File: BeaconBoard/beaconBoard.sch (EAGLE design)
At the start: 32 parts, among them IC1 7805TV, Q1 2N3904

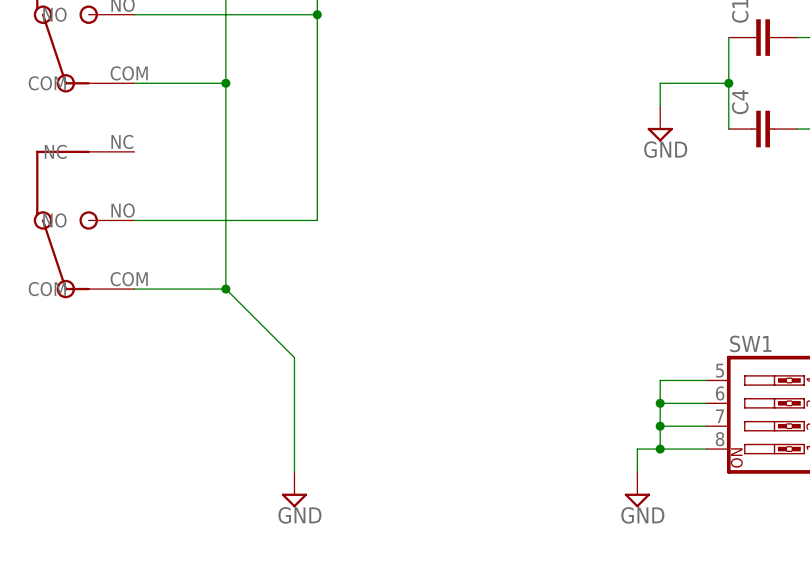
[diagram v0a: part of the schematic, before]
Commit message: Add pull up resistor to bumpers
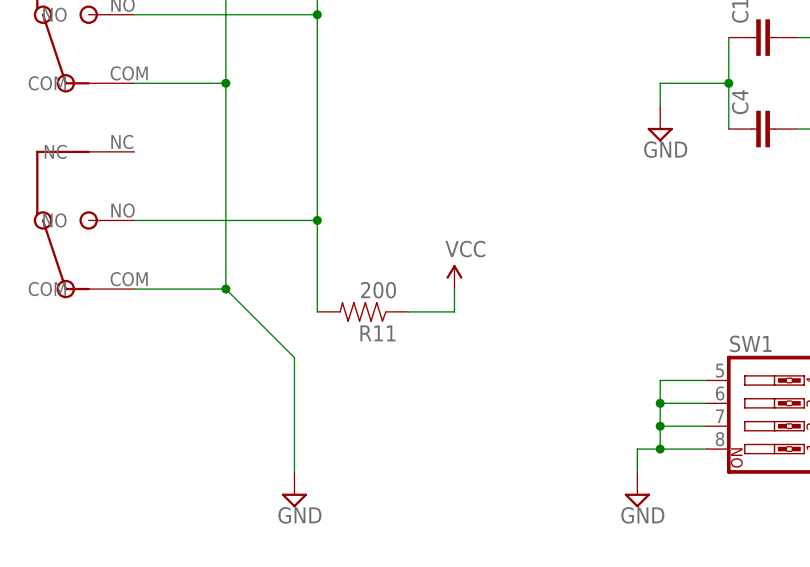
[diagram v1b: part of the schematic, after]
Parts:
- added R11: 200, SparkFun-Resistors:RESISTORPTH-1/4W
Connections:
- net BUMPER: now also R11.2
- net VCC: now also R11.1
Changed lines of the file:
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@@
 <part name="SUPPLY10" library="supply2" deviceset="GND" device=""/>
 <part name="SUPPLY11" library="supply2" deviceset="GND" device=""/>
+<part name="V_OUT6" library="SparkFun-Aesthetics" deviceset="VCC" device=""/>
+<part name="R11" library="SparkFun-Resistors" deviceset="RESISTOR" device="PTH-1/4W" value="200"/>
 </parts>
 <sheets>
@@
 <instance part="SUPPLY10" gate="GND" x="264.16" y="7.62"/>
 <instance part="SUPPLY11" gate="GND" x="17.78" y="-22.86"/>
+<instance part="V_OUT6" gate="1" x="35.56" y="0"/>
+<instance part="R11" gate="G$1" x="25.4" y="-2.54" rot="R180"/>
 </instances>
 <busses>
@@
 <wire x1="198.12" y1="116.84" x2="198.12" y2="114.3" width="0.1524" layer="91"/>
 <junction x="198.12" y="114.3"/>
+</segment>
+<segment>
+<pinref part="R11" gate="G$1" pin="1"/>
+<pinref part="V_OUT6" gate="1" pin="VCC"/>
+<wire x1="30.48" y1="-2.54" x2="35.56" y2="-2.54" width="0.1524" layer="91"/>
+<wire x1="35.56" y1="-2.54" x2="35.56" y2="0" width="0.1524" layer="91"/>
 </segment>
 </net>
@@
 <wire x1="20.32" y1="58.42" x2="38.1" y2="58.42" width="0.1524" layer="91"/>
 <label x="38.1" y="58.42" size="1.778" layer="95"/>
-</segment>
-<segment>
+<pinref part="R11" gate="G$1" pin="2"/>
+<wire x1="20.32" y1="-2.54" x2="20.32" y2="7.62" width="0.1524" layer="91"/>
+<junction x="20.32" y="7.62"/>
+</segment>
+<segment>

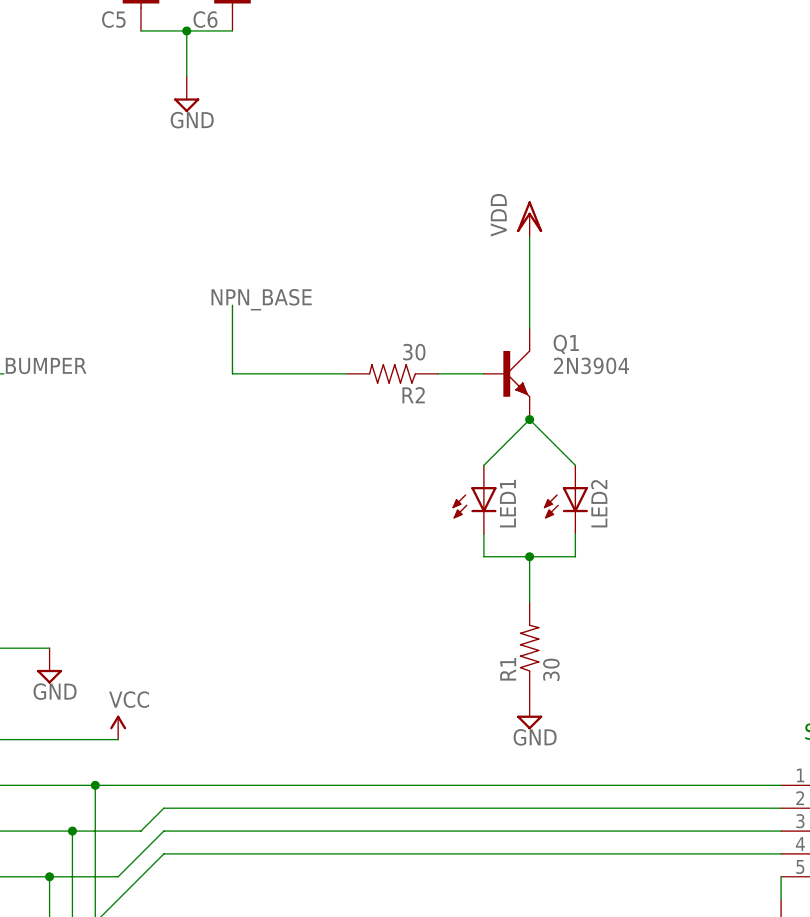
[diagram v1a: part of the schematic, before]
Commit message: Move leds above npn transistor
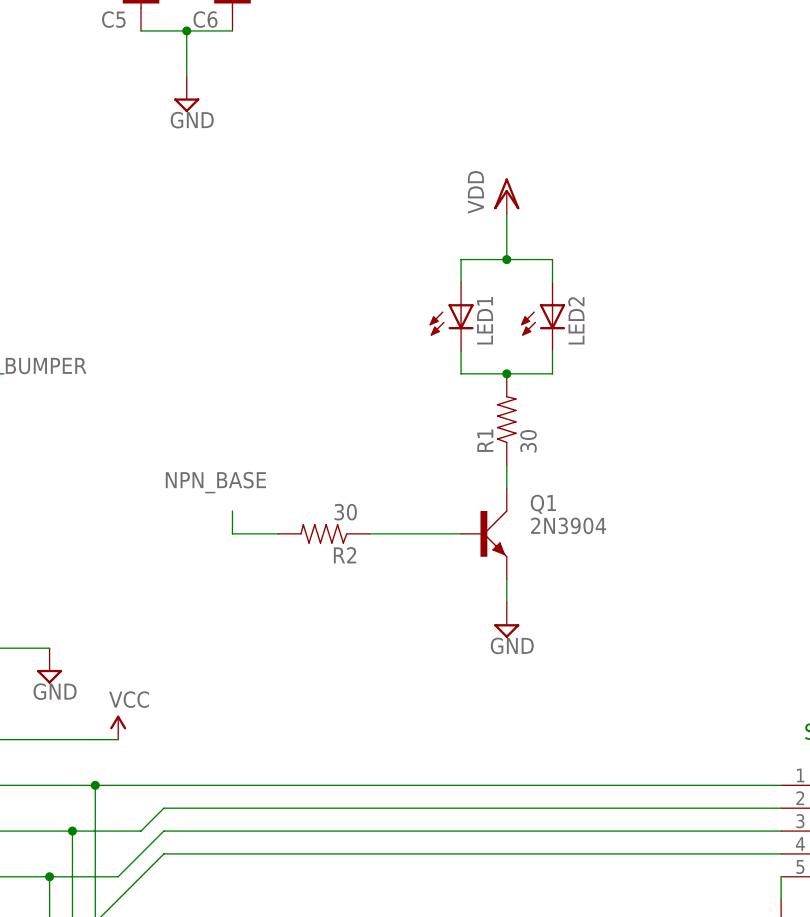
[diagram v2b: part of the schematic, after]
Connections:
- net GND: now also Q1.E; no longer R1.1
- net N$1: now also Q1.C, R1.1; no longer LED1.A, LED2.A, Q1.E
- net VDD: now also LED1.A, LED2.A; no longer Q1.C
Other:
- moved on the sheet: LED1, LED2, Q1, R1, R2
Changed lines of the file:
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@@
 <instance part="U$3" gate="G$1" x="0" y="45.72" rot="R90"/>
 <instance part="U$4" gate="G$1" x="124.46" y="-2.54"/>
-<instance part="Q1" gate="1" x="233.68" y="68.58"/>
+<instance part="Q1" gate="1" x="231.14" y="50.8"/>
 <instance part="J1" gate="G$1" x="-33.02" y="111.76"/>
 <instance part="IC1" gate="A1" x="30.48" y="93.98"/>
@@
 <instance part="V_OUT2" gate="1" x="190.5" y="27.94"/>
 <instance part="SUPPLY3" gate="GND" x="182.88" y="35.56"/>
-<instance part="LED1" gate="G$1" x="231.14" y="55.88"/>
-<instance part="LED2" gate="G$1" x="241.3" y="55.88"/>
-<instance part="SUPPLY4" gate="GND" x="236.22" y="30.48"/>
-<instance part="R1" gate="G$1" x="236.22" y="38.1" rot="R90"/>
-<instance part="R2" gate="G$1" x="220.98" y="68.58" rot="R180"/>
-<instance part="VDD2" gate="G$1" x="236.22" y="86.36"/>
+<instance part="LED1" gate="G$1" x="228.6" y="76.2"/>
+<instance part="LED2" gate="G$1" x="238.76" y="76.2"/>
+<instance part="SUPPLY4" gate="GND" x="233.68" y="40.64"/>
+<instance part="R1" gate="G$1" x="233.68" y="63.5" rot="R90"/>
+<instance part="R2" gate="G$1" x="213.36" y="50.8" rot="R180"/>
+<instance part="VDD2" gate="G$1" x="233.68" y="88.9"/>
 <instance part="R3" gate="G$1" x="193.04" y="-7.62" rot="R180"/>
 <instance part="R4" gate="G$1" x="193.04" y="-15.24" rot="R180"/>
@@
 </segment>
 <segment>
-<pinref part="Q1" gate="1" pin="C"/>
 <pinref part="VDD2" gate="G$1" pin="VDD"/>
-<wire x1="236.22" y1="83.82" x2="236.22" y2="73.66" width="0.1524" layer="91"/>
+<wire x1="233.68" y1="86.36" x2="233.68" y2="81.28" width="0.1524" layer="91"/>
+<wire x1="233.68" y1="81.28" x2="228.6" y2="81.28" width="0.1524" layer="91"/>
+<pinref part="LED1" gate="G$1" pin="A"/>
+<wire x1="228.6" y1="81.28" x2="228.6" y2="78.74" width="0.1524" layer="91"/>
+<pinref part="LED2" gate="G$1" pin="A"/>
+<wire x1="233.68" y1="81.28" x2="238.76" y2="81.28" width="0.1524" layer="91"/>
+<wire x1="238.76" y1="81.28" x2="238.76" y2="78.74" width="0.1524" layer="91"/>
+<junction x="233.68" y="81.28"/>
 </segment>
 </net>
@@
 <pinref part="U$4" gate="G$1" pin="GND@22"/>
 <wire x1="182.88" y1="38.1" x2="172.72" y2="38.1" width="0.1524" layer="91"/>
-</segment>
-<segment>
-<pinref part="SUPPLY4" gate="GND" pin="GND"/>
-<pinref part="R1" gate="G$1" pin="1"/>
 </segment>
 <segment>
@@
 <junction x="10.16" y="22.86"/>
 </segment>
-</net>
-<net name="N$1" class="0">
 <segment>
 <pinref part="Q1" gate="1" pin="E"/>
-<pinref part="LED1" gate="G$1" pin="A"/>
-<wire x1="236.22" y1="63.5" x2="231.14" y2="58.42" width="0.1524" layer="91"/>
-<pinref part="LED2" gate="G$1" pin="A"/>
-<wire x1="236.22" y1="63.5" x2="241.3" y2="58.42" width="0.1524" layer="91"/>
-<junction x="236.22" y="63.5"/>
+<pinref part="SUPPLY4" gate="GND" pin="GND"/>
+<wire x1="233.68" y1="43.18" x2="233.68" y2="45.72" width="0.1524" layer="91"/>
 </segment>
 </net>
@@
 <segment>
 <pinref part="LED1" gate="G$1" pin="C"/>
-<wire x1="231.14" y1="50.8" x2="231.14" y2="48.26" width="0.1524" layer="91"/>
+<wire x1="228.6" y1="71.12" x2="228.6" y2="68.58" width="0.1524" layer="91"/>
 <pinref part="LED2" gate="G$1" pin="C"/>
-<wire x1="241.3" y1="48.26" x2="241.3" y2="50.8" width="0.1524" layer="91"/>
-<wire x1="241.3" y1="48.26" x2="236.22" y2="48.26" width="0.1524" layer="91"/>
+<wire x1="238.76" y1="68.58" x2="238.76" y2="71.12" width="0.1524" layer="91"/>
+<wire x1="238.76" y1="68.58" x2="233.68" y2="68.58" width="0.1524" layer="91"/>
 <pinref part="R1" gate="G$1" pin="2"/>
-<wire x1="236.22" y1="48.26" x2="231.14" y2="48.26" width="0.1524" layer="91"/>
-<wire x1="236.22" y1="43.18" x2="236.22" y2="48.26" width="0.1524" layer="91"/>
-<junction x="236.22" y="48.26"/>
+<wire x1="233.68" y1="68.58" x2="228.6" y2="68.58" width="0.1524" layer="91"/>
+<junction x="233.68" y="68.58"/>
 </segment>
 </net>
@@
 <pinref part="Q1" gate="1" pin="B"/>
 <pinref part="R2" gate="G$1" pin="1"/>
-<wire x1="226.06" y1="68.58" x2="231.14" y2="68.58" width="0.1524" layer="91"/>
+<wire x1="218.44" y1="50.8" x2="228.6" y2="50.8" width="0.1524" layer="91"/>
 </segment>
 </net>
@@
 <segment>
 <pinref part="R2" gate="G$1" pin="2"/>
-<wire x1="215.9" y1="68.58" x2="203.2" y2="68.58" width="0.1524" layer="91"/>
-<wire x1="203.2" y1="68.58" x2="203.2" y2="76.2" width="0.1524" layer="91"/>
-<label x="200.66" y="76.2" size="1.778" layer="95"/>
+<wire x1="208.28" y1="50.8" x2="203.2" y2="50.8" width="0.1524" layer="91"/>
+<wire x1="203.2" y1="50.8" x2="203.2" y2="53.34" width="0.1524" layer="91"/>
+<label x="195.58" y="55.88" size="1.778" layer="95"/>
 </segment>
 </net>
@@
 </segment>
 </net>
+<net name="N$1" class="0">
+<segment>
+<pinref part="Q1" gate="1" pin="C"/>
+<pinref part="R1" gate="G$1" pin="1"/>
+<wire x1="233.68" y1="58.42" x2="233.68" y2="55.88" width="0.1524" layer="91"/>
+</segment>
+</net>
